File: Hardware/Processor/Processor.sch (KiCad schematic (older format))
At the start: 101 parts, among them J1 5V, J2 UART0, J3 USB_OTG, J4 JTAGICE3-SWD, J5 PIOA, J6 PIOB, J7 PIOC, J8 PIOD, Q1 BSSB06NE, Q2 BSSB06NE, Q3 BSSB06NE, Q4 BSSB06NE, SW1 PB, SW2 PB, SW3 ~RST, U1 TXS0102, U2 ATSAM4E16E, U3 3.0V, U4 LM3671, U5 PRTR5V0U2X, Y1 32.768kHz, Y2 12MHz

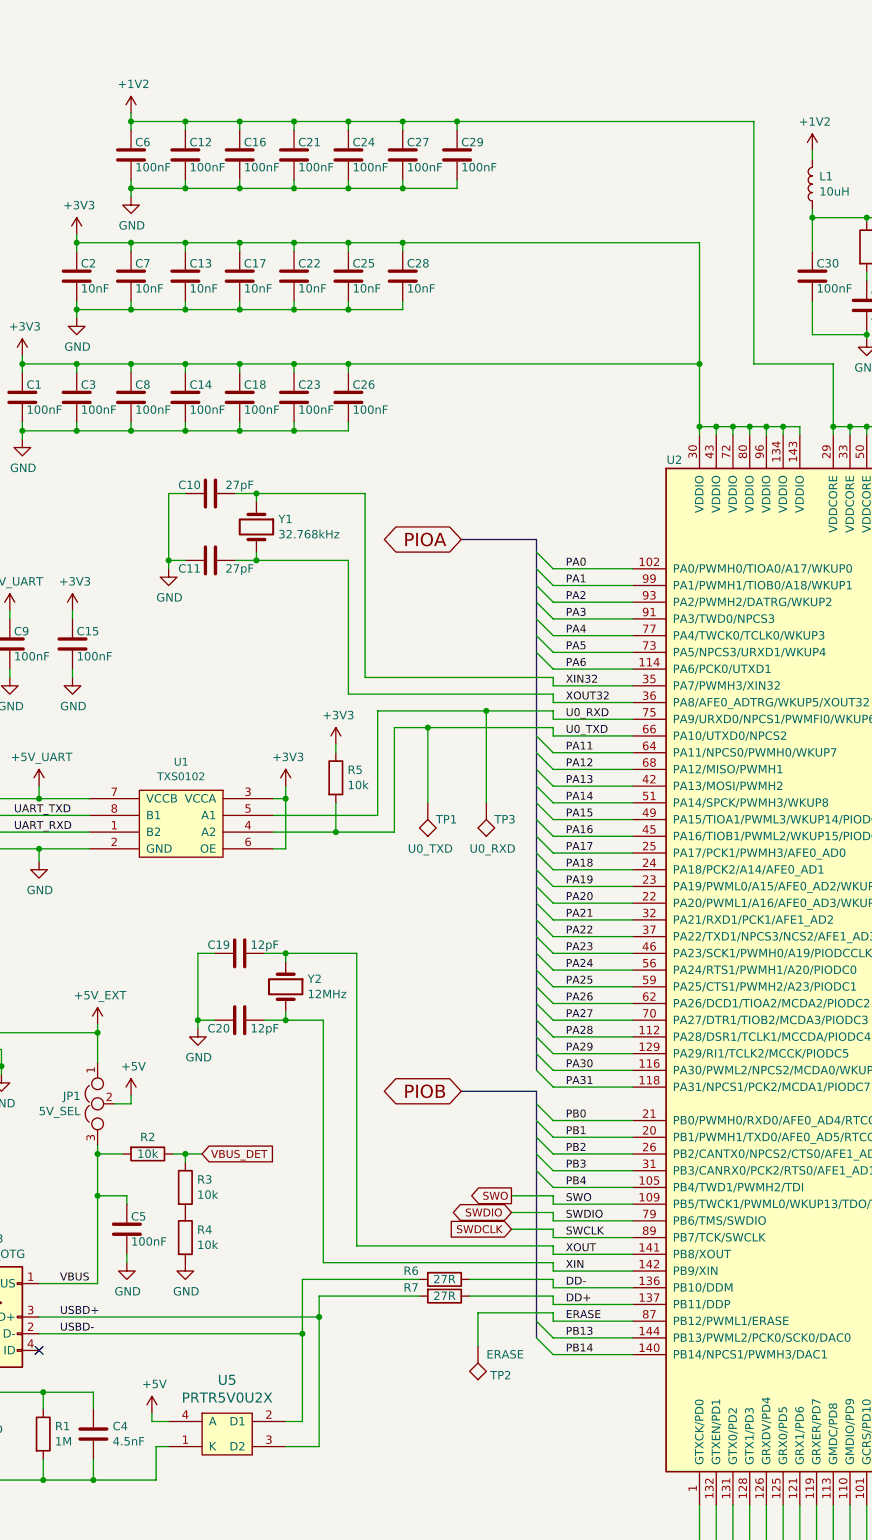
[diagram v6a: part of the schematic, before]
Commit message: Completed initial component placement
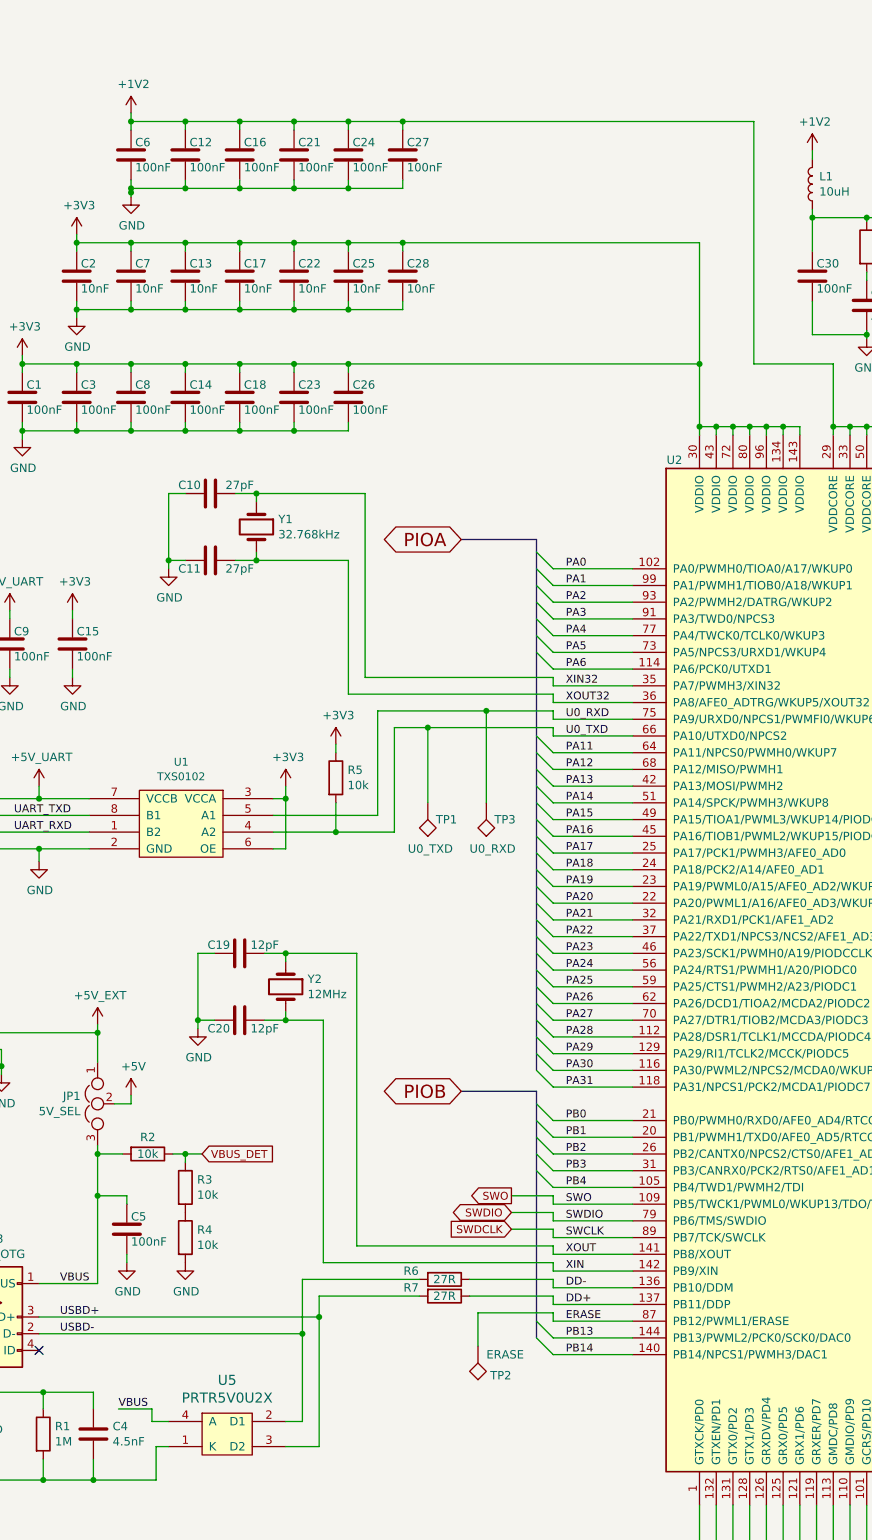
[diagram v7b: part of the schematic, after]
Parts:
- removed C29: 100nF, Capacitors_SMD:C_0603, symbol C
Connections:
- net +5V: no longer U5.4 (A)
- net VBUS: now also U5.4 (A)

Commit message: Started routing
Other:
- moved on the sheet: C19, C20, C40, C41, D5, L2, R22, U4, Y2
